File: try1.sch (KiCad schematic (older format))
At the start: 29 parts, among them J10 Archon-connector-modules-Driv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, J11 Archon-connector-modules-Driv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, J2 Archon-connector-modules-Heat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, J21 DB37, J22 DB37, J3 Archon-connector-modules-Driv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, J31 DB9, J4 Archon-connector-modules-LVBi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, J41 CONN_DVI, J5 Archon-connector-modules-ADC, J6 Archon-connector-modules-ADC, J7 Archon-connector-modules-ADC, J8 Archon-connector-modules-ADC, J9 Archon-connector-modules-HVBi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, P1 CONN_02X02

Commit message: Reassign LV4 Connections
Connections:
- net labels removed: LV4_1, LV4_2, LV4_28, LV4_29, LV4_3, LV4_4
- wire segments 111 -> 141
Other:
- moved on the sheet: J10, J11, J2, J21, J22, J3, J31, J4, J41, J5, J6, J7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

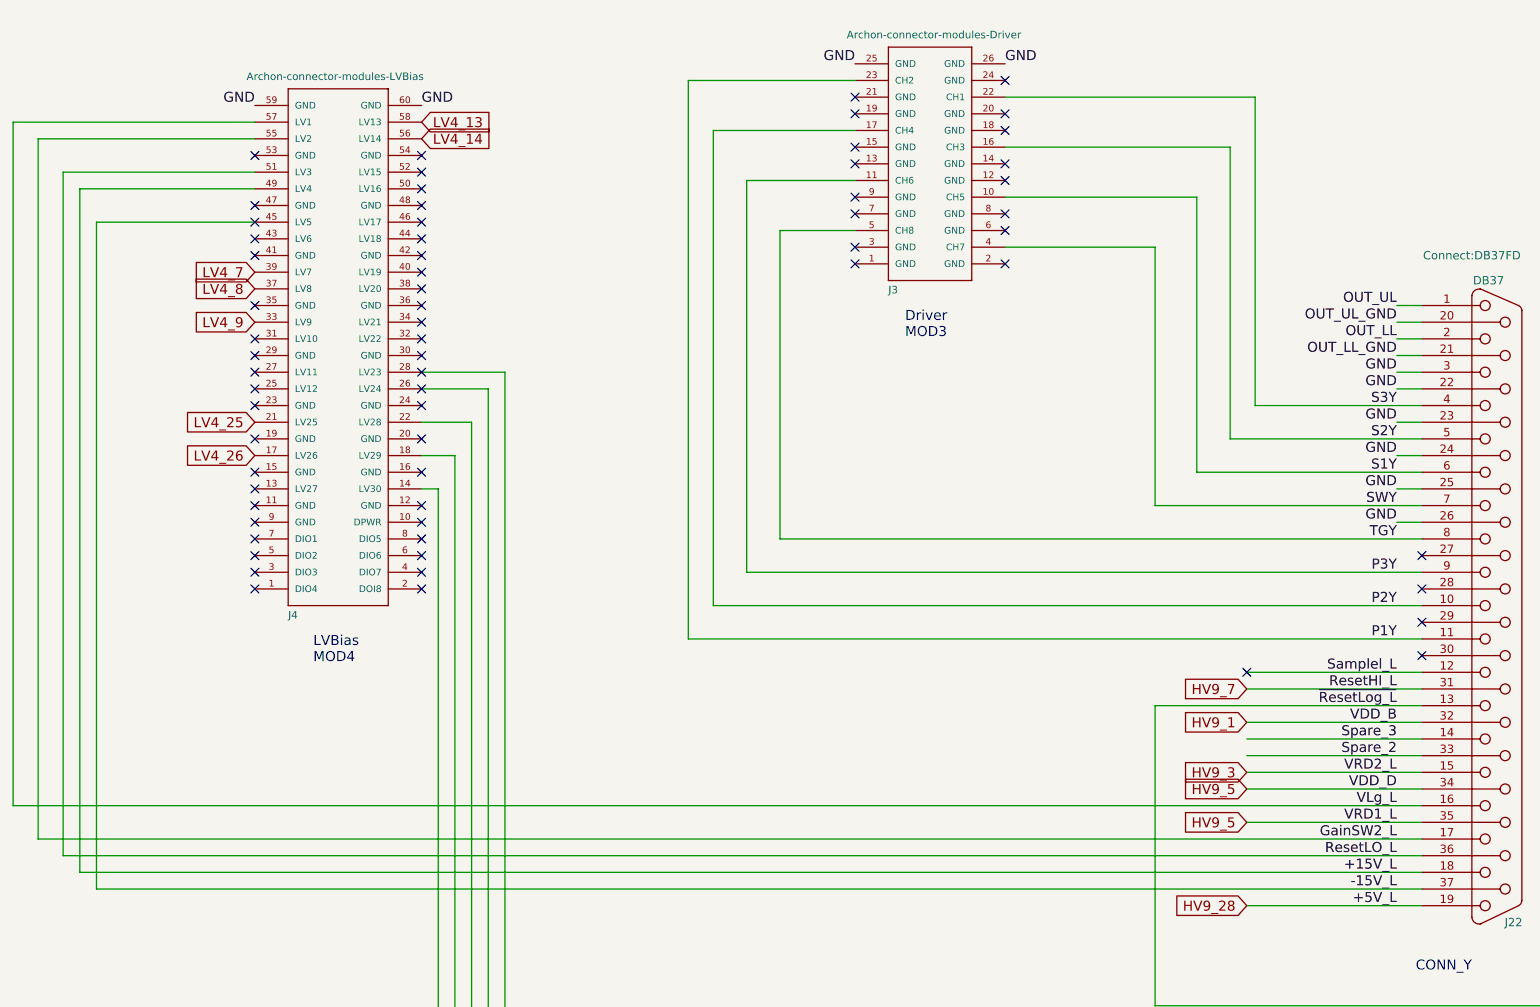
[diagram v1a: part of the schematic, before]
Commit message: Change LV4 Assignments
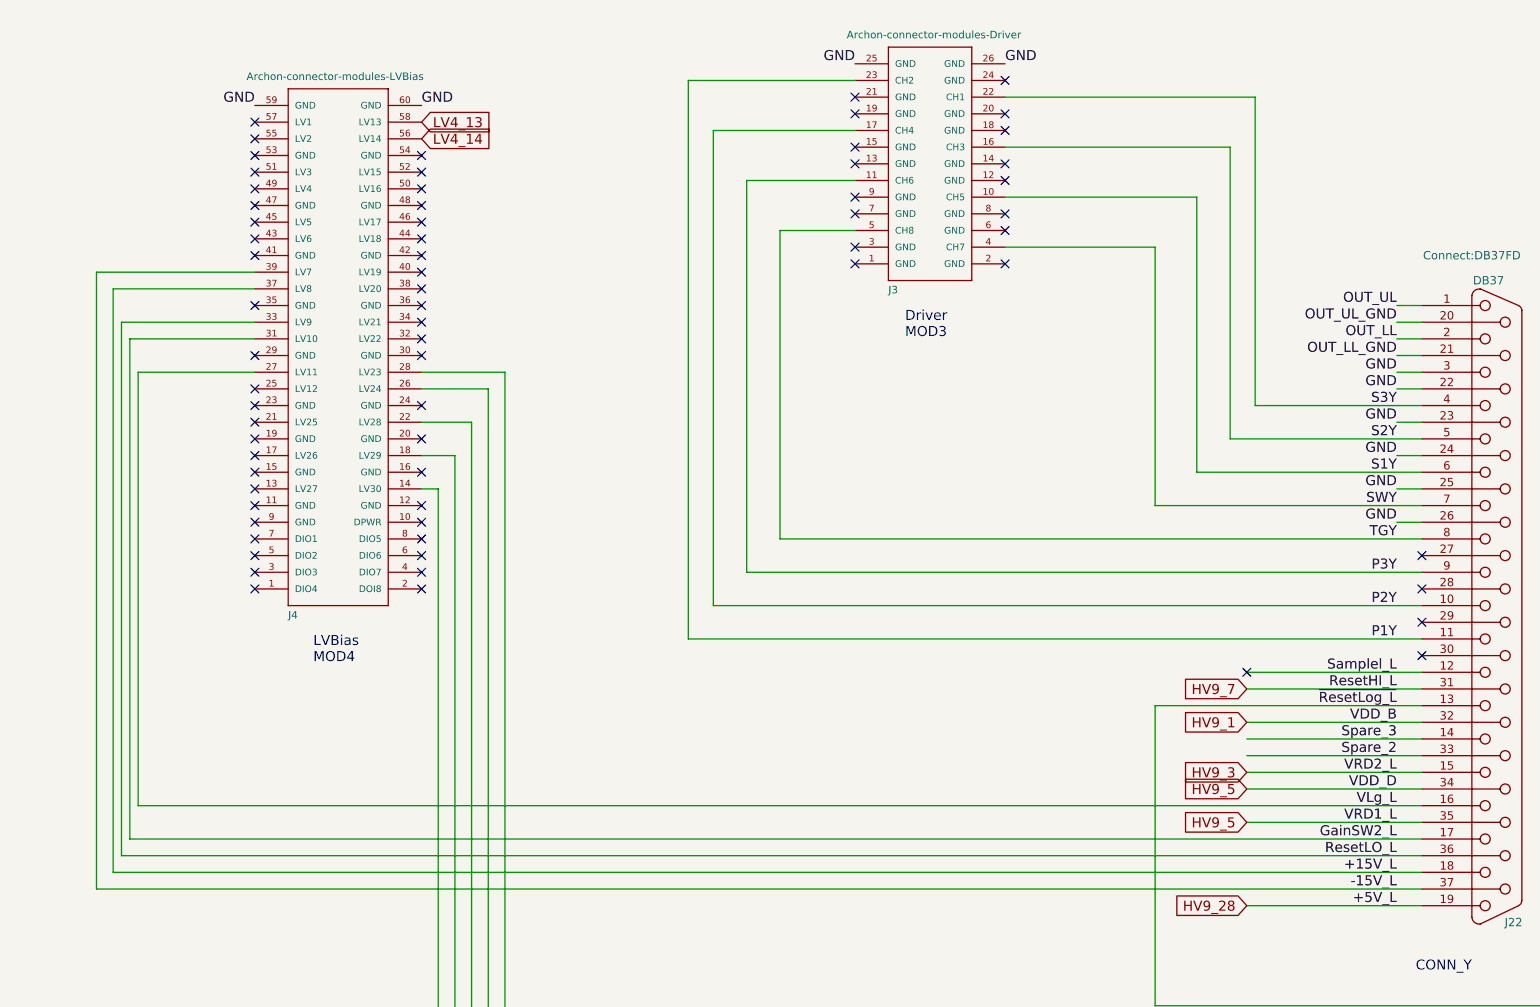
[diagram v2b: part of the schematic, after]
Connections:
- net labels removed: LV4_25, LV4_26
- no-connect marks 311 -> 313
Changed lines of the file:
@@
 Text GLabel 10200 9100 0    60   Input ~ 0
 HV9_7
-Text GLabel 4250 6600 0    60   Input ~ 0
-LV4_7
-Text GLabel 4250 6700 0    60   Input ~ 0
-LV4_8
 $Comp
 L CONN_02X02 P1
@@
 NoConn ~ 4250 6800
 NoConn ~ 4250 7100
-NoConn ~ 4250 7200
 NoConn ~ 4250 7300
 NoConn ~ 4250 7400
@@
 NoConn ~ 5250 7000
 NoConn ~ 5250 7100
-NoConn ~ 5250 7200
-NoConn ~ 5250 7300
 NoConn ~ 5250 7400
 NoConn ~ 5250 7600
@@
 Text GLabel 29300 14050 2    60   Input ~ 0
 LV4_30
-Text GLabel 4250 7700 0    60   Input ~ 0
-LV4_26
-Text GLabel 4250 7500 0    60   Input ~ 0
-LV4_25
 $Comp
 L JUMPER JP1
@@
 Text GLabel 10200 10400 0    60   Input ~ 0
 HV9_28
-NoConn ~ 4250 7000
-Text GLabel 5250 5700 2    60   Input ~ 0
-LV4_13
-Text GLabel 5250 5800 2    60   Input ~ 0
-LV4_14
-Text GLabel 4250 6900 0    60   Input ~ 0
-LV4_9
 NoConn ~ 4250 6400
 NoConn ~ 4250 7900
-NoConn ~ 4250 6300
 NoConn ~ 12300 2900
 NoConn ~ 12300 3000
@@
 	11250 9700 10200 9700
 Wire Wire Line
-	2800 9800 11250 9800
+	3550 9800 11250 9800
 Wire Wire Line
 	11250 9900 10200 9900
 Wire Wire Line
-	2950 10000 11250 10000
-Wire Wire Line
-	3100 10100 11250 10100
-Wire Wire Line
-	3200 10200 11250 10200
+	3500 10000 11250 10000
+Wire Wire Line
+	3450 10100 11250 10100
+Wire Wire Line
+	3400 10200 11250 10200
 Wire Wire Line
 	3300 10300 11250 10300
@@
 	25650 1200 25650 5900
 Wire Wire Line
-	2800 5700 4250 5700
-Wire Wire Line
-	2800 5700 2800 9800
-Wire Wire Line
-	4250 5800 2950 5800
-Wire Wire Line
-	2950 5800 2950 10000
-Wire Wire Line
-	3100 6000 3100 10100
-Wire Wire Line
-	4250 6000 3100 6000
-Wire Wire Line
-	3200 10200 3200 6100
-Wire Wire Line
-	3200 6100 4250 6100
-Wire Wire Line
-	4250 6300 3300 6300
-Wire Wire Line
-	3300 6300 3300 10300
+	3550 7200 3550 9800
+Wire Wire Line
+	3500 7000 3500 10000
+Wire Wire Line
+	3450 6900 3450 10100
+Wire Wire Line
+	3400 10200 3400 6700
+Wire Wire Line
+	3300 6600 3300 10300
 Text Label 18950 10000 2    60   ~ 0
 GainSW2_R
@@
 Wire Wire Line
 	5650 7300 5650 11400
+Wire Wire Line
+	4250 6600 3300 6600
+Wire Wire Line
+	3400 6700 4250 6700
+Wire Wire Line
+	3450 6900 4250 6900
+Wire Wire Line
+	3500 7000 4250 7000
+Wire Wire Line
+	3550 7200 4250 7200
+NoConn ~ 4250 5700
+NoConn ~ 4250 5800
+NoConn ~ 4250 6000
+NoConn ~ 4250 6100
+NoConn ~ 4250 6300
+NoConn ~ 4250 7500
+NoConn ~ 4250 7700
+Text GLabel 5250 5800 2    60   Input ~ 0
+LV4_14
+Text GLabel 5250 5700 2    60   Input ~ 0
+LV4_13
 $EndSCHEMATC

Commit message: Reassign And Complete LV4 Connections
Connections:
- wire segments 141 -> 143
- no-connect marks 313 -> 312
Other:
- moved on the sheet: J5, J6, J7, J8, J9, JP1, JP2, JP3, JP4, W1, W2, W3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

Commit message: Start HVBias Reassigment
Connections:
- net HV9_1: no longer J22.32
- net HV9_25: no longer J9.21 (HV25)
- net HV9_28: no longer J22.19
- net HV9_3: no longer J22.15
- net HV9_5: no longer J22.34, J22.35
- net HV9_6: no longer J9.43 (HV6)
- net HV9_8: no longer J9.37 (HV8)
- net +5V_L: now reaches J9.27 (HV11)
- net +5V_L: now also J22.19
- net VRD1_L: now reaches J9.31 (HV10)
- net VRD1_L: now also J22.35
- net VDD_D: now reaches J9.33 (HV9)
- net VDD_D: now also J22.34
- net HV9_7 renamed ResetHI_L
- net ResetHI_L: now also J9.43 (HV6); no longer J9.39 (HV7)
- new net VDD_B: J22.32, J9.39 (HV7)
- new net VRD2_L: J22.15, J9.37 (HV8)
- no-connect marks 312 -> 318
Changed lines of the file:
@@
 Text GLabel 6000 2300 0    60   Input ~ 0
-HV9_5
-Text GLabel 6000 2400 0    60   Input ~ 0
-HV9_6
-Text GLabel 6000 2600 0    60   Input ~ 0
-HV9_7
-Text GLabel 6000 2700 0    60   Input ~ 0
-HV9_8
-Text GLabel 6000 2000 0    60   Input ~ 0
-HV9_3
-Text GLabel 6000 2100 0    60   Input ~ 0
-HV9_4
-Text GLabel 6000 1700 0    60   Input ~ 0
-HV9_1
-Text GLabel 6000 1800 0    60   Input ~ 0
-HV9_2
-Text GLabel 10200 9300 0    60   Input ~ 0
-HV9_1
-Text GLabel 10200 9600 0    60   Input ~ 0
-HV9_3
-Text GLabel 10200 9700 0    60   Input ~ 0
-HV9_5
-Text GLabel 10200 9900 0    60   Input ~ 0
 HV9_5
 Text GLabel 18350 9300 0    60   Input ~ 0
@@
 Text GLabel 18350 9100 0    60   Input ~ 0
 HV9_8
-Text GLabel 10200 9100 0    60   Input ~ 0
-HV9_7
 $Comp
 L CONN_02X02 P1
@@
 Text GLabel 28550 13850 0    60   Input ~ 0
 LED_PWR
-Text GLabel 6000 3500 0    60   Input ~ 0
-HV9_25
 Text GLabel 6900 3500 2    60   Input ~ 0
 HV9_28
@@
 HV9_25
 NoConn ~ 5250 8100
-Text GLabel 10200 10400 0    60   Input ~ 0
-HV9_28
 NoConn ~ 4250 6400
 NoConn ~ 4250 7900
@@
 	11250 9000 10200 9000
 Wire Wire Line
-	11250 9100 10200 9100
+	6500 9100 11250 9100
 Wire Wire Line
 	9650 9200 11250 9200
 Wire Wire Line
-	11250 9300 10200 9300
+	6550 9300 11250 9300
 Wire Wire Line
 	11250 9400 10200 9400
@@
 	11250 9500 10200 9500
 Wire Wire Line
-	11250 9600 10200 9600
-Wire Wire Line
-	11250 9700 10200 9700
+	6600 9600 11250 9600
+Wire Wire Line
+	6650 9700 11250 9700
 Wire Wire Line
 	3550 9800 11250 9800
 Wire Wire Line
-	11250 9900 10200 9900
+	6700 9900 11250 9900
 Wire Wire Line
 	3500 10000 11250 10000
@@
 	3300 10300 11250 10300
 Wire Wire Line
-	11250 10400 10200 10400
+	6750 10400 11250 10400
 Wire Wire Line
 	19050 6900 18950 6900
@@
 	22850 6450 22850 12200
 NoConn ~ 17150 5550
+Wire Wire Line
+	6000 2400 5500 2400
+Wire Wire Line
+	5500 2400 5500 5250
+Wire Wire Line
+	5500 5250 6500 5250
+Wire Wire Line
+	6500 5250 6500 9100
+Wire Wire Line
+	6000 2600 5550 2600
+Wire Wire Line
+	5550 2600 5550 5200
+Wire Wire Line
+	5550 5200 6550 5200
+Wire Wire Line
+	6550 5200 6550 9300
+Wire Wire Line
+	6000 2700 5600 2700
+Wire Wire Line
+	5600 2700 5600 5150
+Wire Wire Line
+	5600 5150 6600 5150
+Wire Wire Line
+	6600 5150 6600 9600
+Wire Wire Line
+	6000 2900 5650 2900
+Wire Wire Line
+	5650 2900 5650 5100
+Wire Wire Line
+	5650 5100 6650 5100
+Wire Wire Line
+	6650 5100 6650 9700
+Wire Wire Line
+	6000 3000 5700 3000
+Wire Wire Line
+	5700 3000 5700 5050
+Wire Wire Line
+	5700 5050 6700 5050
+Wire Wire Line
+	6700 5050 6700 9900
+Wire Wire Line
+	6000 3200 5750 3200
+Wire Wire Line
+	5750 3200 5750 5000
+Wire Wire Line
+	5750 5000 6750 5000
+Wire Wire Line
+	6750 5000 6750 10400
+NoConn ~ 6000 3500
+NoConn ~ 6000 1700
+NoConn ~ 6000 1800
+NoConn ~ 6000 2000
+NoConn ~ 6000 2100
+NoConn ~ 6000 2300
+Text GLabel 6000 2100 0    60   Input ~ 0
+HV9_4
+Text GLabel 6000 2000 0    60   Input ~ 0
+HV9_3
+Text GLabel 6000 1800 0    60   Input ~ 0
+HV9_2
+Text GLabel 6000 1700 0    60   Input ~ 0
+HV9_1
 $EndSCHEMATC

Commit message: Problem: Lost High Current Assignments
While reassigning pins for the board layout, I forgot that some of
bias modules had different low and high current channels.  I've
tried to recover that in this commit, but it may be wrong.

Also, I changed the orientation of the DB9 header.
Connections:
- net HV9_8 is gone; now on net ResetHI_R: J21.31
- net LV4_7 is gone; now on net SEL_LED_1: J31.7 (P7)
- net LV4_8 is gone; now on net SEL_LED_2: J31.8 (P8)
- net LV4_9 is gone; now on net SHUT_OUT: J31.6 (P6)
- net P2Y is gone; now on net LED_+5: J22.10, J3.17 (CH4)
- net +15V_R: now also J4.32 (LV22); no longer J4.18 (LV29)
- net +5V_L: now also J4.17 (LV26); no longer J9.27 (HV11)
- net -15V_R: now also J4.28 (LV23); no longer J4.14 (LV30)
- net GainSW2_R: now also J4.38 (LV20); no longer J4.26 (LV24)
- net LED_+15V: now also J4.14 (LV30)
- net ResetLO_R: now also J4.34 (LV21); no longer J4.22 (LV28)
- net VLg_R: now also J4.40 (LV19); no longer J4.28 (LV23)
- net SEL_LED_1: now reaches J4.50 (LV16)
- net SEL_LED_2: now reaches J4.52 (LV15)
- net SHUT_OUT: now reaches J9.52 (HV15)
- net HV9_1 renamed ResetHI_R
- net HV9_2 renamed VDD_A
- net HV9_25 renamed +5V_R
- net +5V_R: now also J9.14 (HV30)
- net HV9_28 renamed LED_PWR
- net LED_PWR: now also J31.2
- net HV9_29 renamed LED_+5
- net HV9_3 renamed VRD2_R
- net VRD2_R: now also J21.15
- removed net HV9_30: J31.2, J9.14 (HV30)
- net HV9_4 renamed VDD_C
- net VDD_C: now also J21.34; no longer J21.15
- net HV9_5 renamed VRD1_R
- net VRD1_R: now also J21.35
- removed net HV9_6: J21.34, J21.35
- net LV4_13: no longer names the net of J4.58 (LV13)
- net LV4_14: no longer names the net of J4.56 (LV14)
- no-connect marks 318 -> 307
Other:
- moved on the sheet: J10, J11, J21, J22, J3, J31, J4, J5, J6, J7, J8, J9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
